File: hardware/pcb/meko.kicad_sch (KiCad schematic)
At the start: 1 part, among them U1 SAMA7D65-4HB

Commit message: split apart the sama7 sybmol into units
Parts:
- added unit 6 of U1
- added unit 2 of U1
- added unit 3 of U1
- added unit 4 of U1
- added unit 5 of U1
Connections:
- net GND: now reaches U1.A1 (GND), U1.A11 (GND), U1.A14 (GND), U1.A17 (GND), U1.A21 (GND), U1.AA1 (GND), U1.AA11 (GND), U1.AA14 (GND), U1.AA17 (GND), U1.AA21 (GND), U1.AA8 (GND), U1.AA9 (GND), U1.B6 (GND), U1.C4 (GND), U1.C7 (GND), U1.D13 (GND), U1.D9 (GND), U1.E15 (GND), U1.E21 (GND), U1.F16 (GND), U1.G15 (GND), U1.G17 (GND), U1.H14 (GND), U1.H21 (GND), U1.H8 (GND), U1.H9 (GND), U1.J18 (GND), U1.J4 (GND), U1.K11 (GND), U1.L1 (GND), U1.L11 (GND), U1.L15 (GND), U1.L21 (GND), U1.N18 (GND), U1.N4 (GND), U1.P1 (GND), U1.P14 (GND), U1.P21 (GND), U1.P8 (GND), U1.R11 (GND), U1.R17 (GND), U1.R5 (GND), U1.R7 (GND), U1.T17 (GND), U1.T5 (GND), U1.U1 (GND), U1.U21 (GND), U1.U7 (GND), U1.V13 (GND), U1.W5 (GND)
- net GND: now also U1.E1 (GNDANA), U1.E7 (GNDANA), U1.G11 (GNDBAT), U1.G5 (GNDIN33), U1.H1 (GNDANA), U1.L7 (GNDUTMI), U1.R15 (GNDDPHY), U1.U15 (GNDDPHY), U1.V9 (GNDANA)

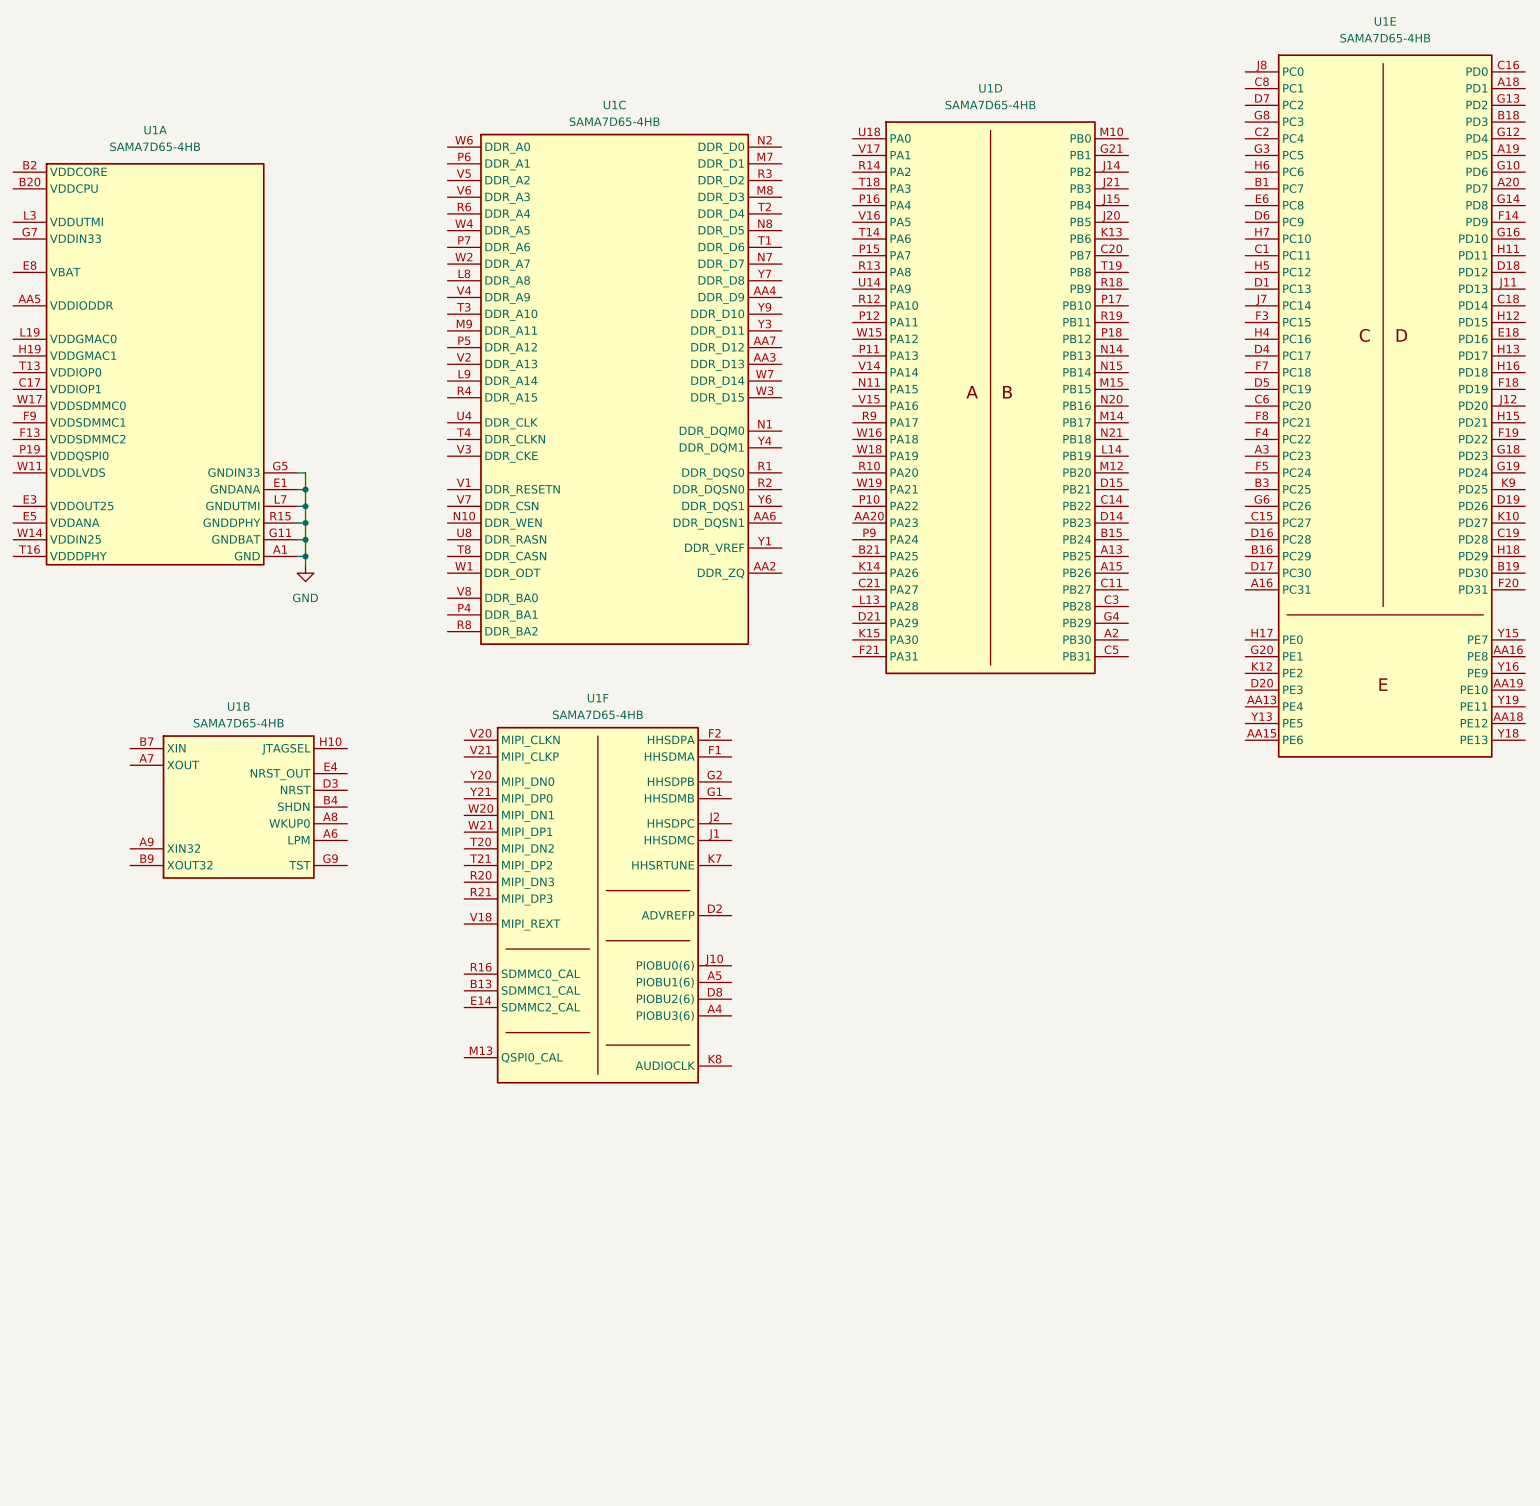
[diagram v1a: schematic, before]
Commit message: made mcp16502 symbol
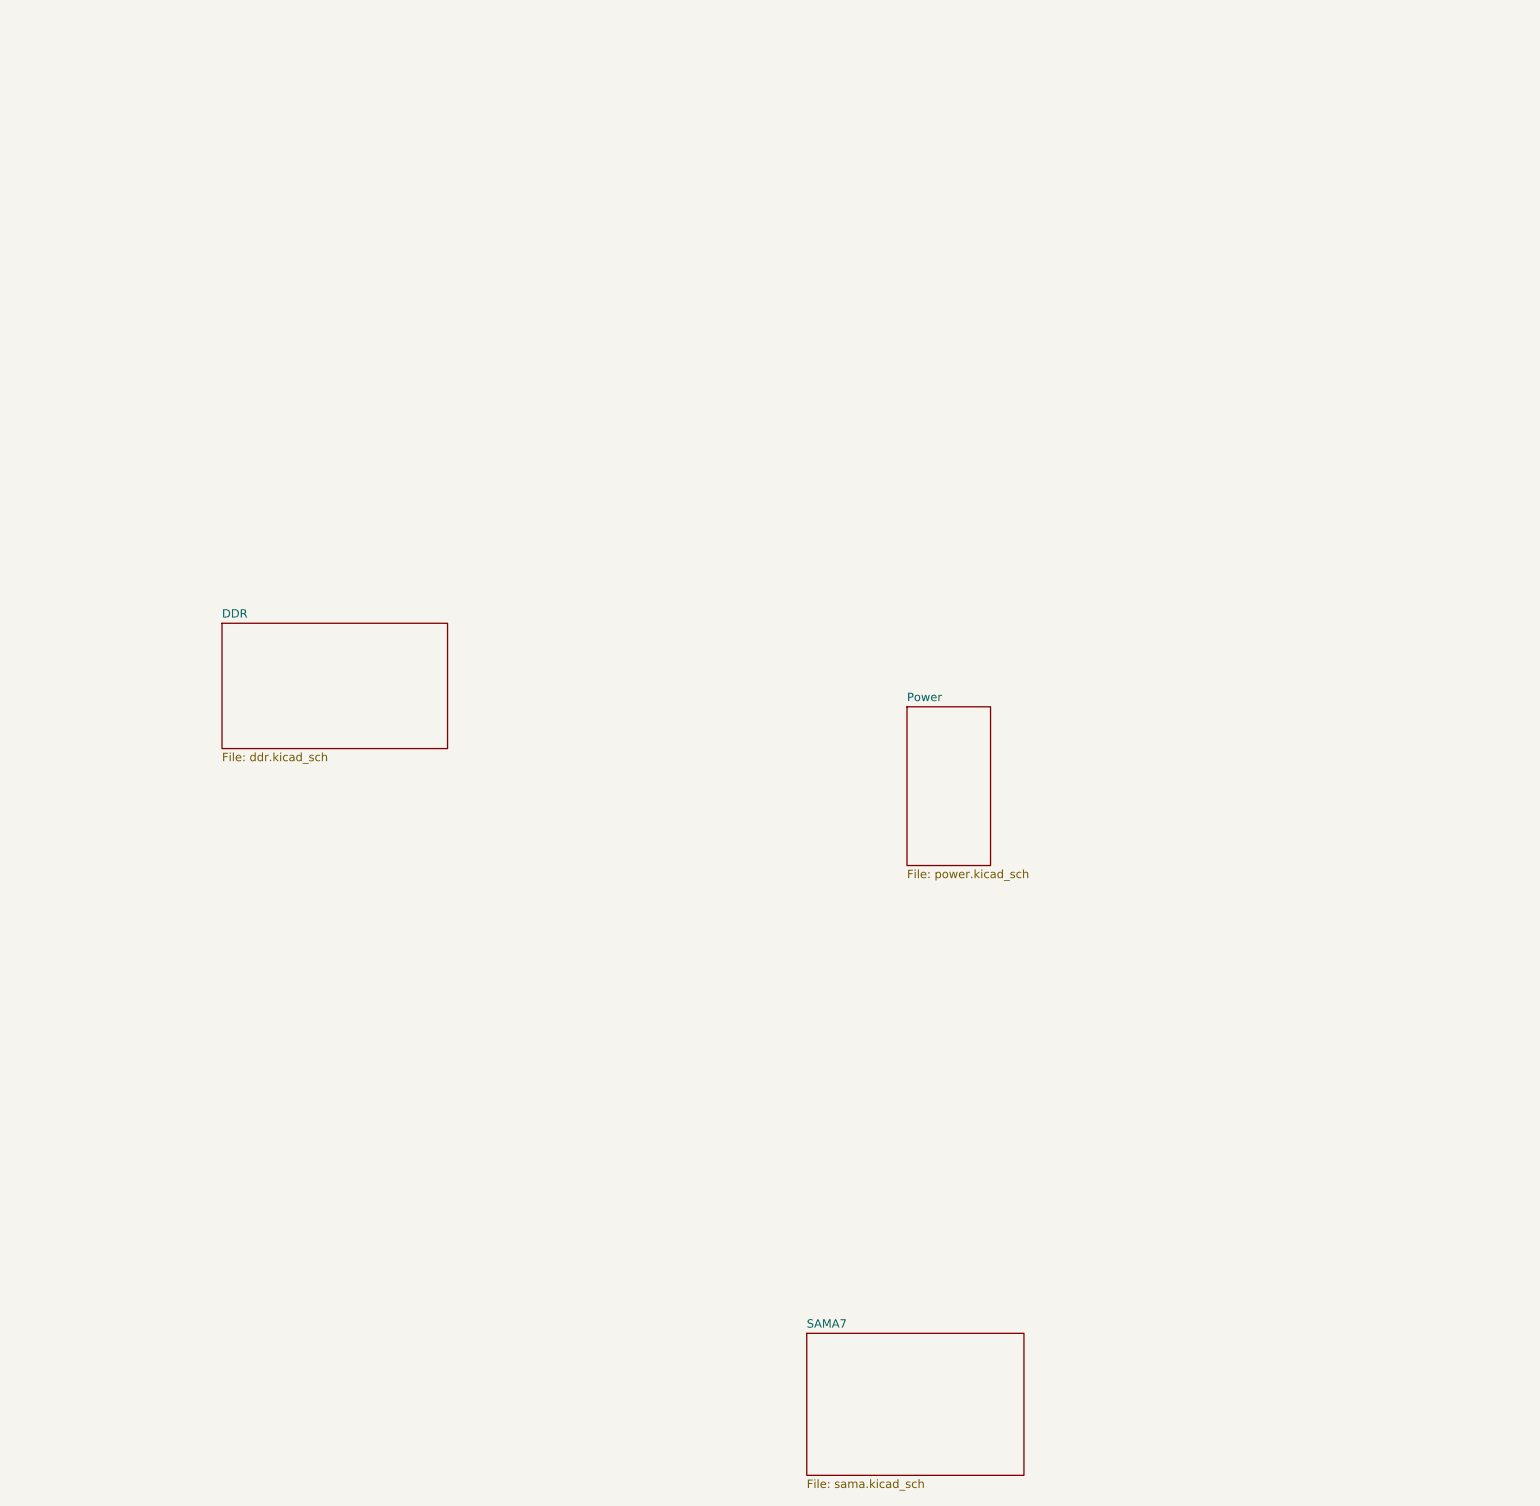
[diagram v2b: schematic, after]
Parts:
- removed U1: SAMA7D65-4HB, SAMA7D65-4HB:Microchip_4HB_TFBGA-343_14x14mm_Layout21x21_P0.65mm, symbol SAMA7D65-4HB:SAMA7D65-4HB
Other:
- added sheet DDR (ddr.kicad_sch)
- added sheet Power (power.kicad_sch)
- added sheet SAMA7 (sama.kicad_sch)

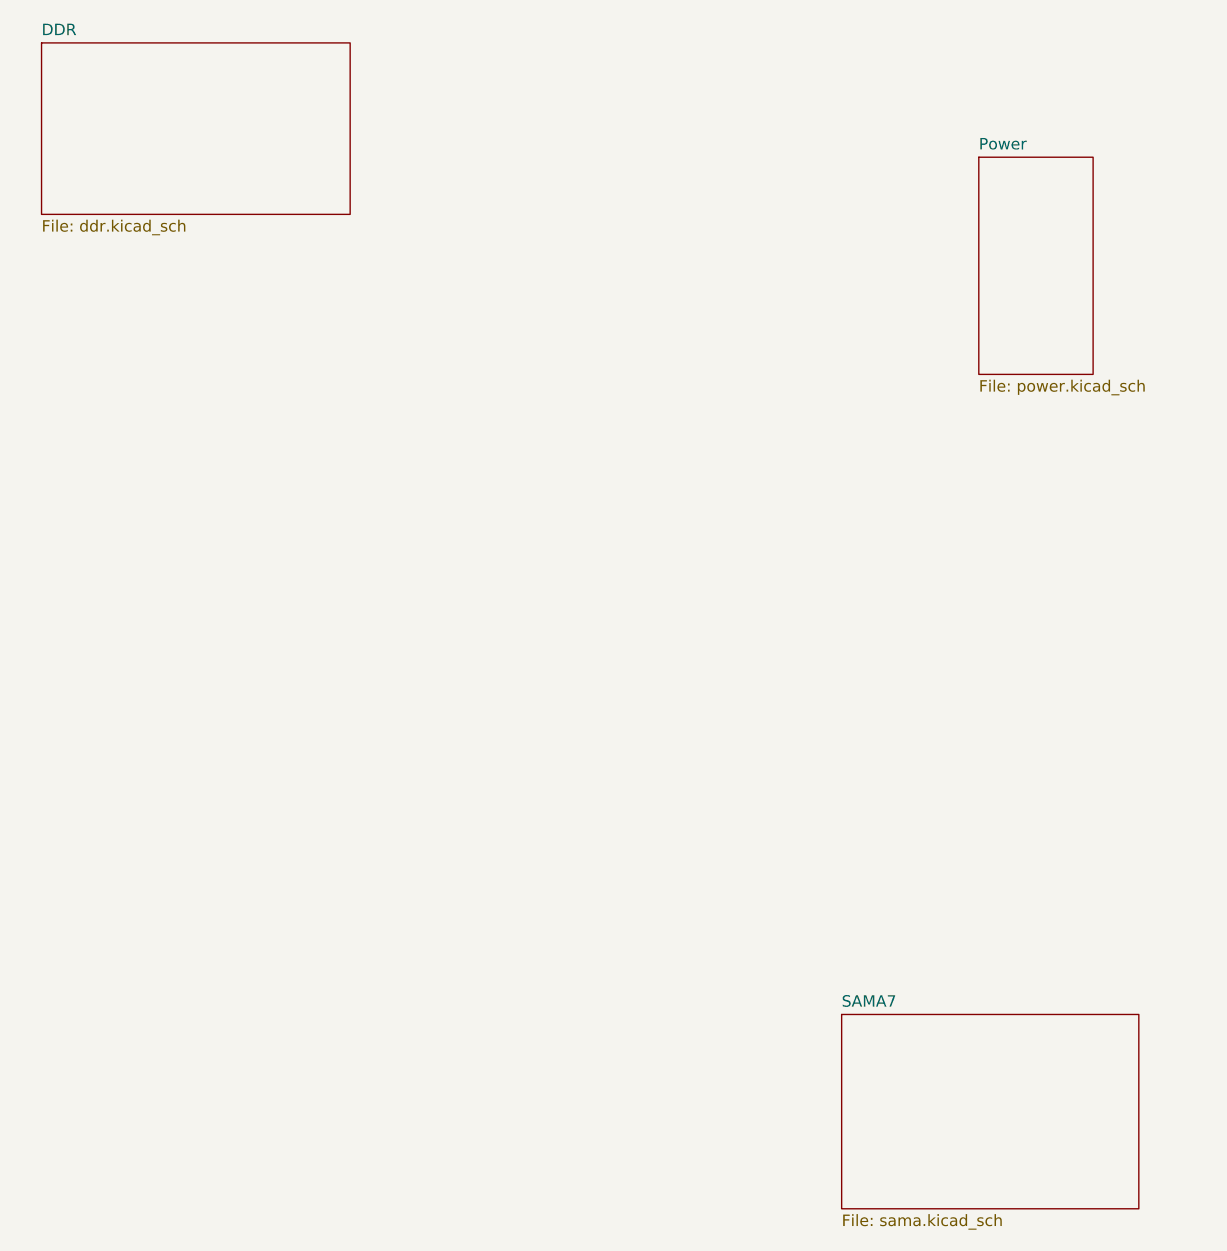
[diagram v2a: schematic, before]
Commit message: connected ddr to sama7, still need to do pwr
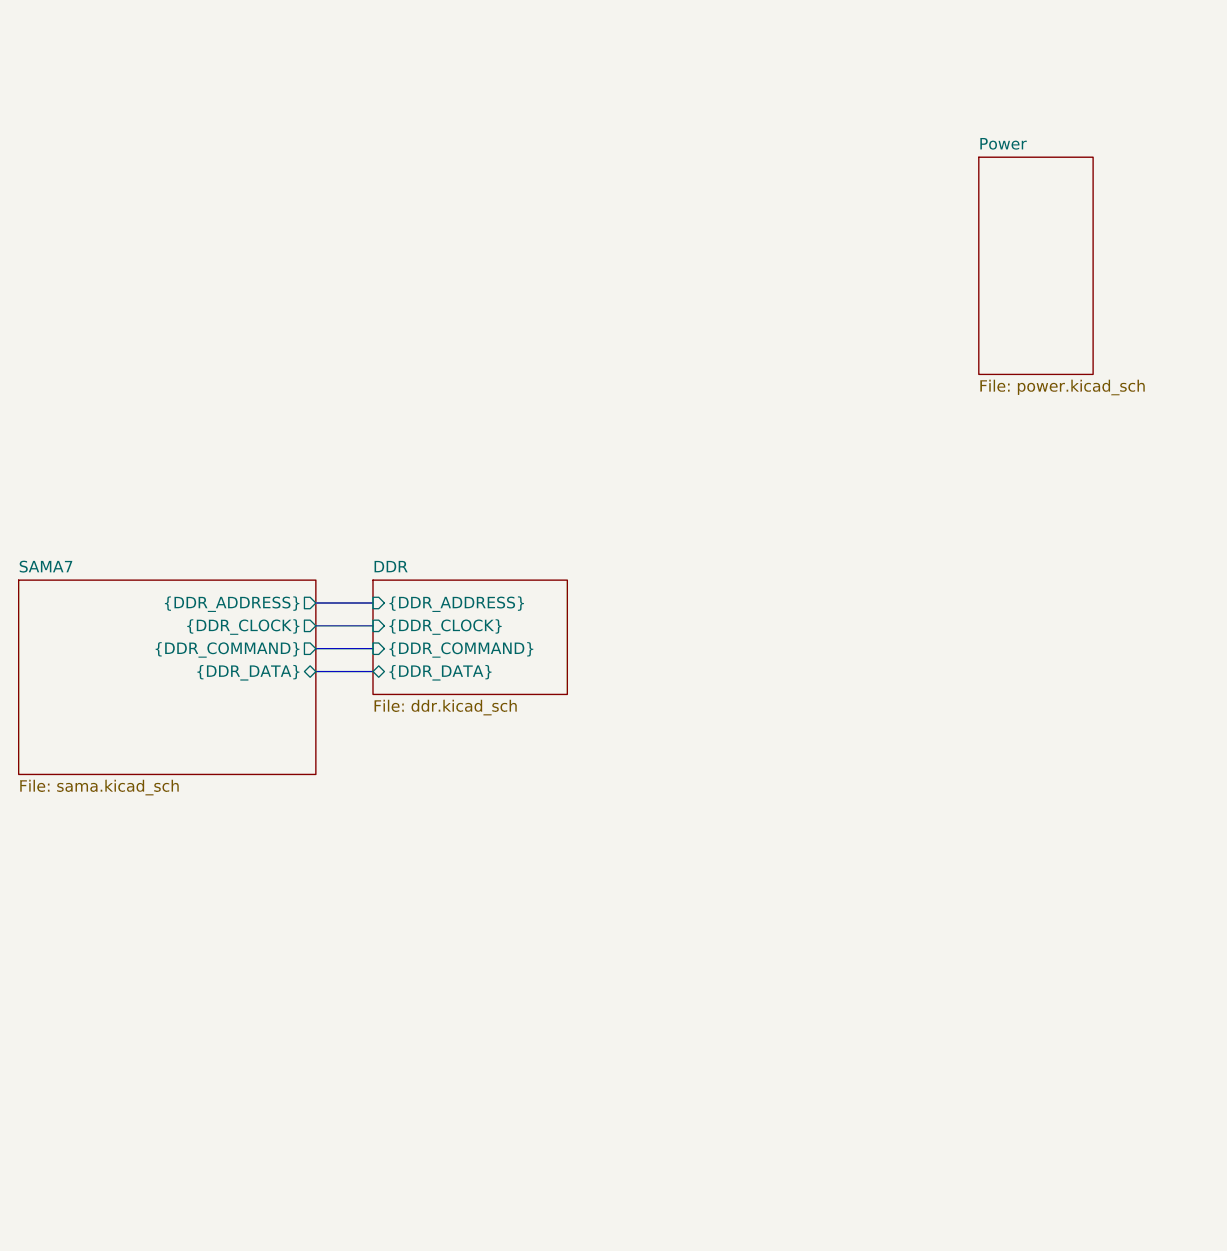
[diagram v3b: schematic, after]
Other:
- sheet DDR ports: added {DDR_ADDRESS}, {DDR_CLOCK}, {DDR_COMMAND}, {DDR_DATA}; removed none
- sheet SAMA7 ports: added {DDR_ADDRESS}, {DDR_CLOCK}, {DDR_COMMAND}, {DDR_DATA}; removed none
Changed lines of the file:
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@@
 	(generator_version "10.0")
 	(paper "A3")
+	(bus
+		(pts
+			(xy 147.32 176.53) (xy 153.67 176.53)
+		)
+		(stroke
+			(width 0)
+			(type default)
+		)
+	)
+	(bus
+		(pts
+			(xy 147.32 181.61) (xy 153.67 181.61)
+		)
+		(stroke
+			(width 0)
+			(type default)
+		)
+	)
+	(bus
+		(pts
+			(xy 147.32 173.99) (xy 153.67 173.99)
+		)
+		(stroke
+			(width 0)
+			(type default)
+		)
+	)
+	(bus
+		(pts
+			(xy 147.32 179.07) (xy 153.67 179.07)
+		)
+		(stroke
+			(width 0)
+			(type default)
+		)
+	)
 	(sheet
-		(at 205.74 219.71)
+		(at 114.3 171.45)
 		(size 33.02 21.59)
 		(exclude_from_sim no)
@@
 		)
 		(property "Sheetname" "SAMA7"
-			(at 205.74 218.9984 0)
+			(at 114.3 170.7384 0)
 			(show_name no)
 			(do_not_autoplace no)
@@
 		)
 		(property "Sheetfile" "sama.kicad_sch"
-			(at 205.74 241.8846 0)
+			(at 114.3 193.6246 0)
 			(show_name no)
 			(do_not_autoplace no)
@@
 				)
 				(justify left top)
+			)
+		)
+		(pin "{DDR_ADDRESS}" output
+			(at 147.32 173.99 0)
+			(effects
+				(font
+					(size 1.27 1.27)
+				)
+				(justify right)
+			)
+		)
+		(pin "{DDR_CLOCK}" output
+			(at 147.32 176.53 0)
+			(effects
+				(font
+					(size 1.27 1.27)
+				)
+				(justify right)
+			)
+		)
+		(pin "{DDR_COMMAND}" output
+			(at 147.32 179.07 0)
+			(effects
+				(font
+					(size 1.27 1.27)
+				)
+				(justify right)
+			)
+		)
+		(pin "{DDR_DATA}" bidirectional
+			(at 147.32 181.61 0)
+			(effects
+				(font
+					(size 1.27 1.27)
+				)
+				(justify right)
 			)
 		)
@@
 	)
 	(sheet
-		(at 116.84 111.76)
-		(size 34.29 19.05)
+		(at 153.67 171.45)
+		(size 21.59 12.7)
 		(exclude_from_sim no)
 		(in_bom yes)
@@
 		)
 		(property "Sheetname" "DDR"
-			(at 116.84 111.0484 0)
+			(at 153.67 170.7384 0)
 			(show_name no)
 			(do_not_autoplace no)
@@
 		)
 		(property "Sheetfile" "ddr.kicad_sch"
-			(at 116.84 131.3946 0)
+			(at 153.67 184.7346 0)
 			(show_name no)
 			(do_not_autoplace no)
@@
 			)
 		)
+		(pin "{DDR_ADDRESS}" input
+			(at 153.67 173.99 180)
+			(effects
+				(font
+					(size 1.27 1.27)
+				)
+				(justify left)
+			)
+		)
+		(pin "{DDR_CLOCK}" input
+			(at 153.67 176.53 180)
+			(effects
+				(font
+					(size 1.27 1.27)
+				)
+				(justify left)
+			)
+		)
+		(pin "{DDR_COMMAND}" input
+			(at 153.67 179.07 180)
+			(effects
+				(font
+					(size 1.27 1.27)
+				)
+				(justify left)
+			)
+		)
+		(pin "{DDR_DATA}" bidirectional
+			(at 153.67 181.61 180)
+			(effects
+				(font
+					(size 1.27 1.27)
+				)
+				(justify left)
+			)
+		)
